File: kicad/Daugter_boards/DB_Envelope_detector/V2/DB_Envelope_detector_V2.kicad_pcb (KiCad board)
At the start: 2 copper layers, 30.5 x 50.8 mm, 12 parts, among them P1 CONN_01X19, P2 CONN_01X19, T1 2N2222, T2 2N2907A, T3 2N2907A

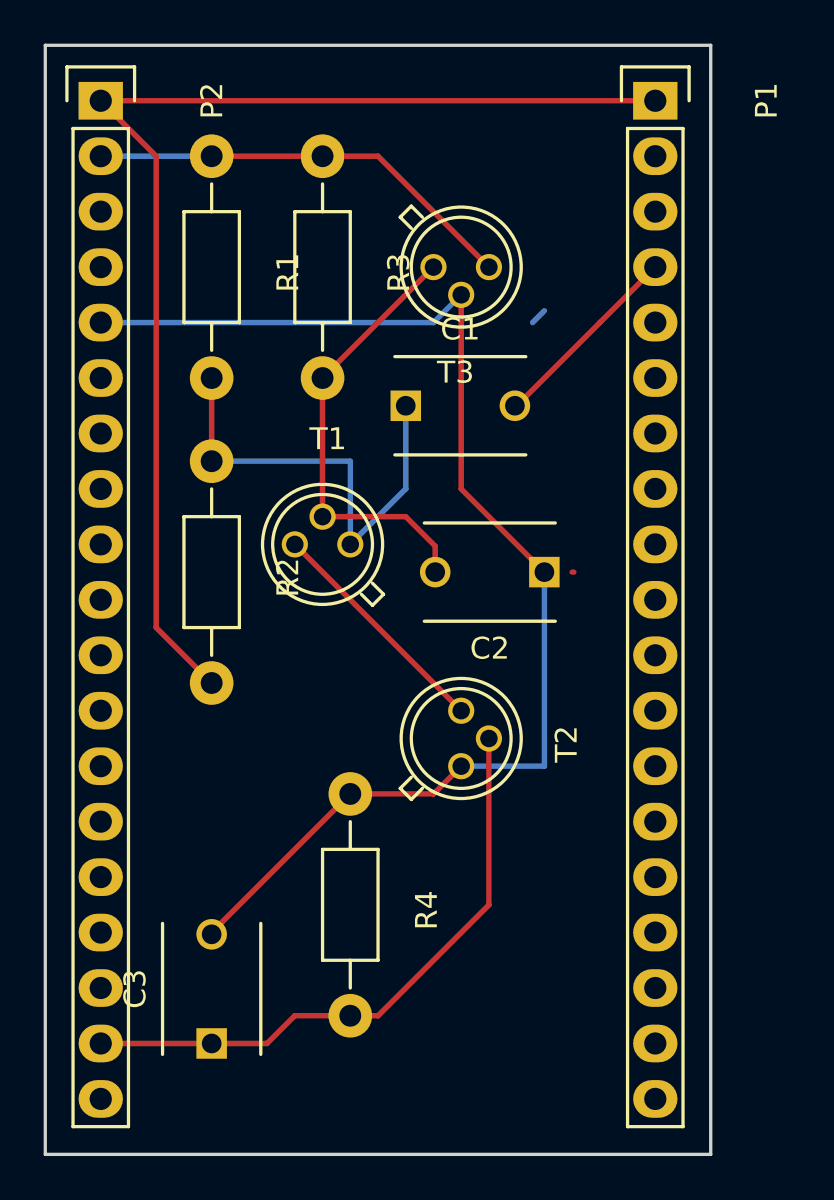
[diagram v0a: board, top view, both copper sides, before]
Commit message: update DB_Envelope_Detector with correct librairy and footprint
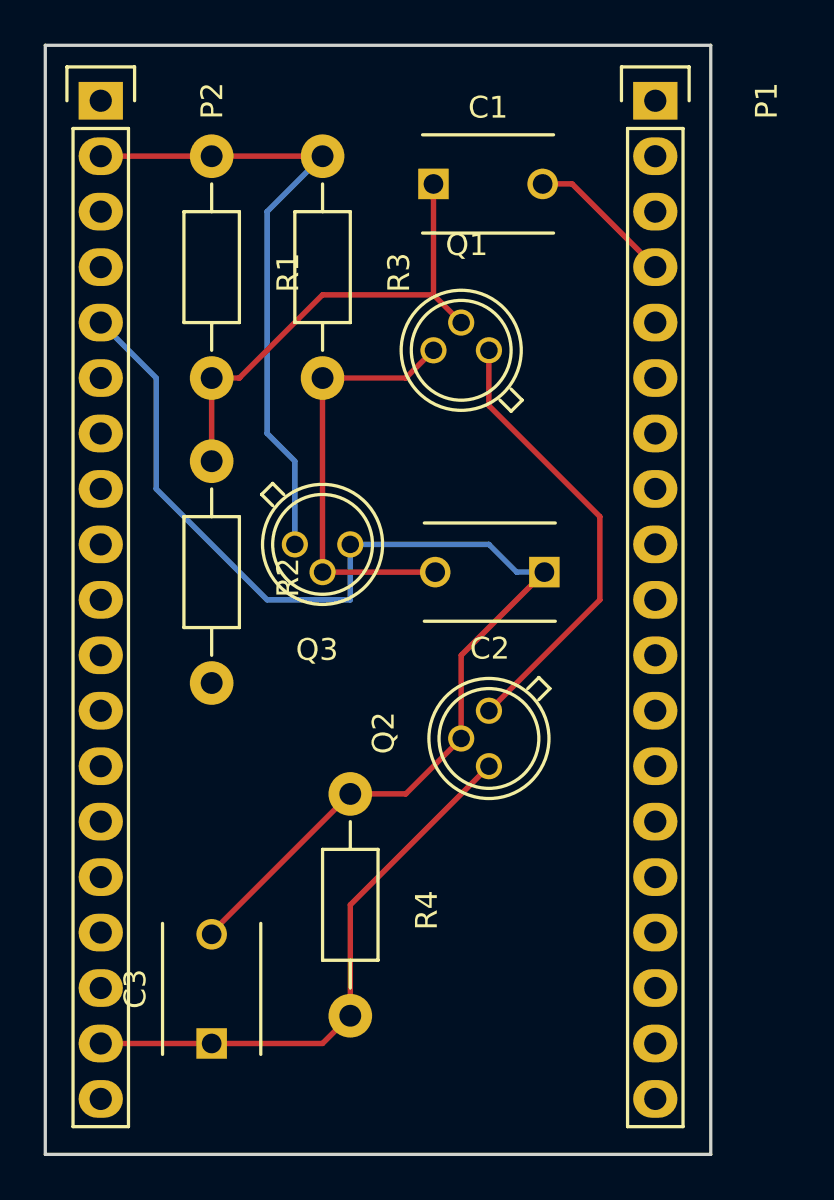
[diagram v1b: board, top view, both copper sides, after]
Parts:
- removed T1: 2N2222, TO_SOT_Packages_THT:TO-18_3Pin
- removed T2, T3: 2N2907A, TO_SOT_Packages_THT:TO-18_3Pin
- added Q1: Q2N2222, TO_SOT_Packages_THT:TO-18_3Pin, F.Cu at (77.5, 81.3)
- added Q2: Q2N2907, TO_SOT_Packages_THT:TO-18_3Pin, F.Cu at (78.7, 99.1)
- added Q3: Q2N2907, TO_SOT_Packages_THT:TO-18_3Pin, F.Cu at (71.1, 90.2)
- moved C1 10.2 mm to (76.2, 73.7)
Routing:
- net GND: track 54.2 -> 0.00 mm
- net Net-(Q1-Pad1): track 0.00 -> 20.7 mm
- net Net-(T1-Pad3): track 10.8 -> 0.00 mm
- net Net-(P2-Pad2): track 19.9 -> 29.5 mm
- net Net-(C2-Pad1): track 58.7 -> 56.0 mm
- net Net-(C1-Pad2): track 9.06 -> 6.74 mm
- net Net-(C3-Pad1): track 28.0 -> 26.0 mm
- net Net-(C1-Pad1): track 21.4 -> 22.4 mm
- net (no net): track 0.84 -> 0.00 mm
- net Net-(C2-Pad2): track 20.4 -> 19.7 mm
- net Net-(P1-Pad14): track 0.73 -> 0.00 mm

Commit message: update librairy with correct nomenclature of transistor
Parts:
- Q1: value Q2N2222 -> 2N2222
- Q2, Q3: value Q2N2907 -> 2N2907
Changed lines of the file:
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@@
       (effects (font (size 1 1) (thickness 0.15)))
     )
-    (fp_text value Q2N2222 (at 0 4.826) (layer F.Fab)
+    (fp_text value 2N2222 (at 0 4.826) (layer F.Fab)
       (effects (font (size 1 1) (thickness 0.15)))
     )
@@
       (effects (font (size 1 1) (thickness 0.15)))
     )
-    (fp_text value Q2N2907 (at 0 4.826 90) (layer F.Fab)
+    (fp_text value 2N2907 (at 0 4.826 90) (layer F.Fab)
       (effects (font (size 1 1) (thickness 0.15)))
     )
@@
       (effects (font (size 1 1) (thickness 0.15)))
     )
-    (fp_text value Q2N2907 (at 0 4.826 180) (layer F.Fab)
+    (fp_text value 2N2907 (at 0 4.826 180) (layer F.Fab)
       (effects (font (size 1 1) (thickness 0.15)))
     )
